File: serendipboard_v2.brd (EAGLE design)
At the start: 34.3 x 48.3 mm, 85 parts, among them IC1 TP4056, IC2 DW01A, IC3 DS3231/SO, J4 USB3076-XX-X_REVC, Q1 FS8205A, Q2 MMBT2222ALT1G, Q3 RUC002N05HZGT116, Q4 DMG3415U, Q5 MMBT2222ALT1G, Q7 RUC002N05HZGT116, Q8 MBT3904DW1T1G, U1 MAX17043, U2 MIC5219 3.3V, U4 9DoF IMU, U5 ESP32-WROOM-32D, U6 FT231XQ-R, U7 MIC5219 3.3V

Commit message: .
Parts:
- renumbered JP1 to VCC, JP2 to AD0, LS1 to BUZZER, S1 to BOOT, S2 to RST, S3 to BTN1, S4 to BTN2, S5 to PWR
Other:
- board text added: "B+"
- board text added: "B-"

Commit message: .
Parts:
- added D2: LTST-C19HE1WT, LTST-C19HE1WT:LED_LTST-C19HE1WT
- added R25, R29, R30: 220, rcl:R0402
- BTN1, BTN2, PWR: value KMR731NGLFS -> (none); device KMR731NGLFS:SW_KMR731NGLFS -> SparkFun-Connectors:1X02
- moved B1 17.9 mm to (12.2, 41.3), turned to 0 degrees
- moved PWR 9.69 mm to (29.6, 29.3), turned to 0 degrees
- moved BTN2 7.42 mm to (29.6, 35.2), turned to 0 degrees
- moved R28 7.03 mm to (20.3, 37.0), turned to 180 degrees
- moved RST 6.10 mm to (30.4, 25.0)
- moved R27 5.72 mm to (20.3, 35.9), turned to 180 degrees
- moved BOOT 5.59 mm to (30.4, 19.8), turned to 270 degrees
- moved BTN1 4.66 mm to (29.6, 32.3), turned to 0 degrees
- moved R26 4.62 mm to (20.3, 34.9), turned to 0 degrees
- moved R9 3.64 mm to (20.3, 38.0), turned to 180 degrees
- moved R19 3.24 mm to (20.3, 33.0), turned to 0 degrees
- moved R20 2.88 mm to (20.3, 34.0), turned to 0 degrees
- moved R13 1.09 mm to (4.70, 35.9), turned to 90 degrees
- moved Q5 0.63 mm to (2.54, 35.6)
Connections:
- new net N$24: D2.1, R25.2
- new net N$26: D2.2, R29.2
- new net N$27: D2.3, R30.2
- net GND: now also BTN1.2, BTN2.2, D2.4, PWR.2; no longer BTN1.3, BTN1.4, BTN2.3, BTN2.4, PWR.3, PWR.4
- net GPIO15: no longer BTN2.2
- net GPIO27: no longer BTN1.2
- net PWR: no longer PWR.2
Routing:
- net GND: track 290.9 -> 238.2 mm, vias 18 -> 16
- net PWR: track 50.3 -> 0.00 mm, vias 4 -> 0
- net EN: track 76.8 -> 34.2 mm, vias 6 -> 5
- net SDA: track 106.7 -> 64.8 mm, vias 6 -> 5
- net GPIO27: track 38.2 -> 2.68 mm, vias 6 -> 1
- net GPIO15: track 48.1 -> 14.3 mm, vias 5 -> 2
- net SCL: track 115.5 -> 89.3 mm
- net VCC: track 91.0 -> 74.9 mm
- net RXD: track 30.4 -> 21.0 mm
- net 3.3V_ESP: track 38.8 -> 29.7 mm
- net MOTOR: track 12.7 -> 8.53 mm
- net N$9: track 4.74 -> 1.14 mm
- net QST: track 64.7 -> 61.4 mm
- net N$13: track 2.14 -> 0.00 mm
- net IO0: track 25.7 -> 24.2 mm
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
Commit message: .
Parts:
- moved R19 0.23 mm to (20.3, 32.8)
- moved R20 0.18 mm to (20.3, 33.9)
- moved R9 0.08 mm to (20.3, 38.0)
- moved R25 0.05 mm to (30.6, 38.4)
- moved R28 0.05 mm to (20.3, 37.0)
- turned R27 to 0 degrees
- turned R30 to 0 degrees
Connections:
- new net BLUE: R30.1, U5.30
- new net GREEN: R29.1, U5.29
- new net N$28: BTN1.1, R28.1
- new net RED: R25.1, U5.28
- net GPIO27: no longer BTN1.1, R28.1
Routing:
- net GPIO27: track 2.68 -> 91.5 mm, vias 1 -> 6
- net GND: track 238.2 -> 305.4 mm, vias 16 -> 18
- net SDA: track 64.8 -> 119.0 mm, vias 5 -> 9
- net EN: track 34.2 -> 66.6 mm, vias 5 -> 9
- net PWR: track 0.00 -> 31.3 mm, vias 0 -> 2
- net N$9: track 1.14 -> 30.4 mm, vias 0 -> 4
- net SCL: track 89.3 -> 117.1 mm, vias 7 -> 11
- net BLUE: track 0.00 -> 24.9 mm, vias 0 -> 2
- net RED: track 0.00 -> 20.3 mm, vias 0 -> 4
- net VCC: track 74.9 -> 90.8 mm
- net 3.3V_ESP: track 29.7 -> 45.5 mm, vias 1 -> 3
- net GREEN: track 0.00 -> 14.7 mm
- net GPIO15: track 14.3 -> 26.6 mm, vias 2 -> 1
- net RXD: track 21.0 -> 29.7 mm, vias 2 -> 3
- net N$24: track 0.00 -> 5.25 mm
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
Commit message: .
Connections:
- removed net N$28: BTN1.1, R28.1
- net GPIO27: now also BTN1.1, R28.1
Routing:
- net GPIO27: track 91.5 -> 94.3 mm
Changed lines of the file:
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@@
 <wire x1="5.2435" y1="24.284" x2="4.7625" y2="24.765" width="0.254" layer="16"/>
 <wire x1="10.09390625" y1="28.2575" x2="6.12040625" y2="24.284" width="0.254" layer="16"/>
+<contactref element="R28" pad="1"/>
+<contactref element="BTN1" pad="1"/>
+<wire x1="19.82" y1="37.0078" x2="19.00295625" y2="37.0078" width="0.254" layer="16"/>
+<wire x1="29.591" y1="32.258" x2="30.988" y2="33.655" width="0.254" layer="1"/>
 </signal>
 <signal name="GPIO15">
@@
 <wire x1="30.107" y1="38.4209875" x2="30.107" y2="38.4302" width="0.254" layer="1"/>
 </signal>
-<signal name="N$28">
-<contactref element="R28" pad="1"/>
-<contactref element="BTN1" pad="1"/>
-<wire x1="19.82" y1="37.0078" x2="29.591" y2="32.258" width="0" layer="19" extent="16-16"/>
-</signal>
 </signals>

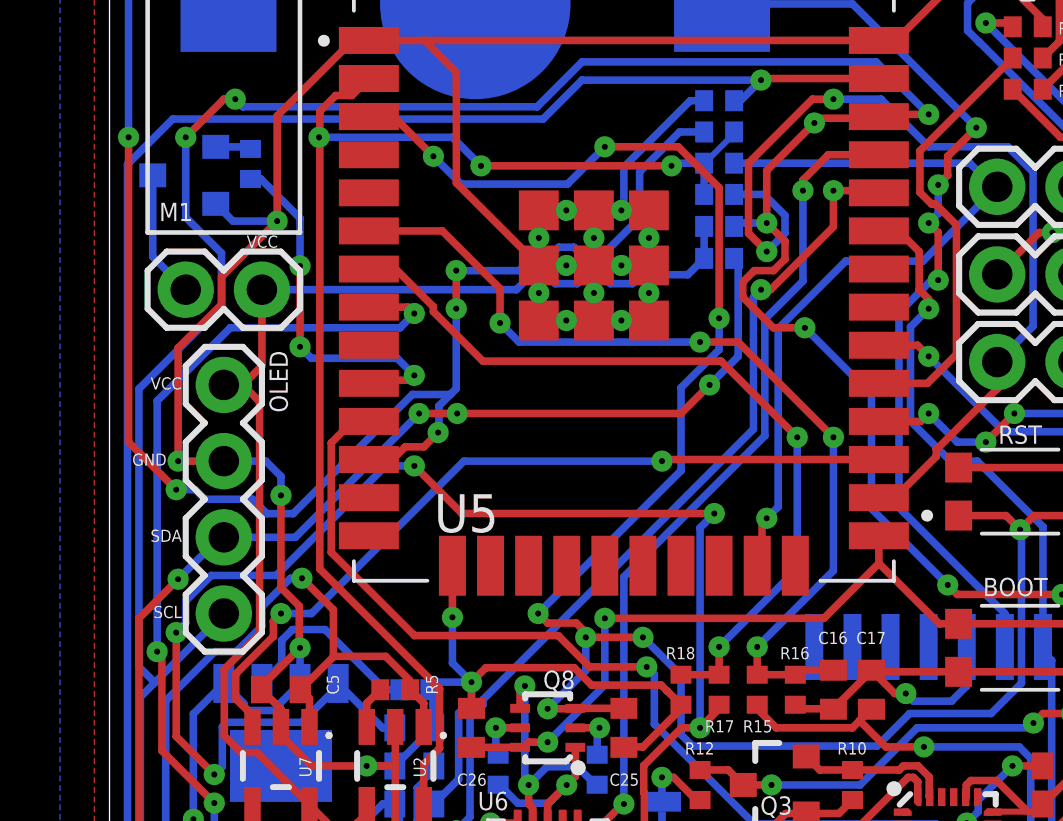
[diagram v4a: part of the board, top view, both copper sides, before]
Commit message: Update serendipboard_v2.brd
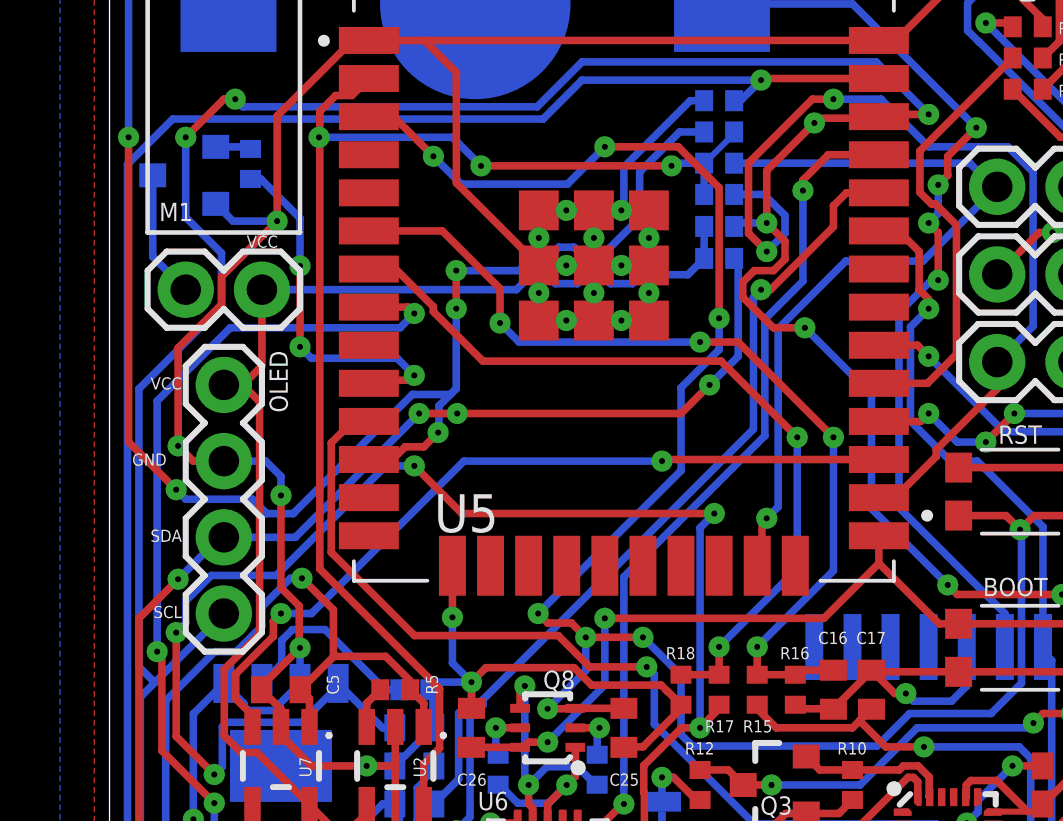
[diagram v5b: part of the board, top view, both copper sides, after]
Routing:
- net RXD: track 29.7 -> 29.3 mm, vias 3 -> 2
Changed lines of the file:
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@@
 <wire x1="5.588" y1="34.036" x2="3.7338" y2="32.1818" width="0.254" layer="1"/>
 <wire x1="3.7338" y1="32.1818" x2="3.7338" y2="31.25550625" width="0.254" layer="1"/>
-<wire x1="2.286" y1="29.80770625" x2="2.286" y2="26.035" width="0.254" layer="1"/>
+<wire x1="2.286" y1="29.80770625" x2="2.286" y2="26.543" width="0.254" layer="1"/>
 <wire x1="3.7338" y1="31.25550625" x2="2.286" y2="29.80770625" width="0.254" layer="1"/>
-<via x="2.286" y="26.035" extent="1-16" drill="0.2"/>
-<wire x1="2.286" y1="26.035" x2="3.81" y2="26.035" width="0.254" layer="1"/>
+<via x="2.286" y="26.543" extent="1-16" drill="0.2"/>
+<wire x1="2.794" y1="26.035" x2="3.81" y2="26.035" width="0.254" layer="1"/>
+<wire x1="2.794" y1="26.035" x2="2.286" y2="26.543" width="0.254" layer="1"/>
 <wire x1="17.0625" y1="30.723" x2="17.98" y2="30.723" width="0.254" layer="1"/>
 <wire x1="10.66" y1="18.415" x2="10.914" y2="18.669" width="0.254" layer="16"/>
@@
 <wire x1="14.2875" y1="20.955" x2="19.05" y2="25.7175" width="0.254" layer="16"/>
 <wire x1="14.605" y1="20.6375" x2="14.2875" y2="20.955" width="0.254" layer="1"/>
-<wire x1="15.5575" y1="20.6375" x2="14.605" y2="20.6375" width="0.254" layer="1"/>
-<wire x1="15.875" y1="20.32" x2="15.5575" y2="20.6375" width="0.254" layer="1"/>
-<wire x1="15.875" y1="20.32" x2="15.875" y2="20.16125" width="0.254" layer="1"/>
 <via x="10.795" y="36.195" extent="1-16" drill="0.2"/>
 <via x="16.51" y="36.5125" extent="1-16" drill="0.2"/>
@@
 <wire x1="15.267" y1="35.2695" x2="11.7205" y2="35.2695" width="0.254" layer="16"/>
 <wire x1="11.7205" y1="35.2695" x2="10.795" y2="36.195" width="0.254" layer="16"/>
+<wire x1="15.875" y1="20.16125" x2="15.39875" y2="20.6375" width="0.254" layer="1"/>
+<wire x1="15.39875" y1="20.6375" x2="14.605" y2="20.6375" width="0.254" layer="1"/>
 </signal>
 <signal name="IO0">
@@
 <via x="11.557" y="13.716" extent="1-16" drill="0.2"/>
 <wire x1="11.557" y1="13.716" x2="12.017" y2="14.176" width="0.254" layer="16"/>
-<via x="24.13" y="35.052" extent="1-16" drill="0.2"/>
 <wire x1="12.017" y1="14.176" x2="12.017" y2="17.478" width="0.254" layer="16"/>
-<wire x1="24.13" y1="35.052" x2="25.571" y2="35.052" width="0.254" layer="1"/>
-<wire x1="25.571" y1="35.052" x2="25.645" y2="34.978" width="0.254" layer="1"/>
 <wire x1="12.017" y1="17.478" x2="12.446" y2="17.907" width="0.254" layer="16"/>
 <wire x1="12.446" y1="17.907" x2="12.446" y2="18.0840875" width="0.254" layer="16"/>
@@
 <via x="21.717" y="31.75" extent="1-16" drill="0.2"/>
 <wire x1="21.717" y1="31.75" x2="22.0361625" y2="31.75" width="0.254" layer="1"/>
-<wire x1="22.0361625" y1="31.75" x2="24.13" y2="33.8438375" width="0.254" layer="1"/>
-<wire x1="24.13" y1="33.8438375" x2="24.13" y2="35.052" width="0.254" layer="1"/>
+<wire x1="24.13" y1="33.8438375" x2="22.0361625" y2="31.75" width="0.254" layer="1"/>
+<wire x1="24.13" y1="34.544" x2="24.13" y2="33.8438375" width="0.254" layer="1"/>
+<wire x1="24.13" y1="34.544" x2="24.564" y2="34.978" width="0.254" layer="1"/>
+<wire x1="24.564" y1="34.978" x2="25.645" y2="34.978" width="0.254" layer="1"/>
 </signal>
 <signal name="N$15">
@@
 <wire x1="10.98075" y1="27.0145" x2="10.95375" y2="26.9875" width="0.254" layer="16"/>
 <wire x1="11.557" y1="28.45059375" x2="11.396953125" y2="28.290546875" width="0.254" layer="16"/>
-<wire x1="11.396953125" y1="28.290546875" x2="10.98075" y2="27.87434375" width="0.254" layer="16"/>
+<wire x1="11.36390625" y1="28.2575" x2="10.98075" y2="27.87434375" width="0.254" layer="16"/>
 <wire x1="10.98075" y1="27.87434375" x2="10.98075" y2="27.0145" width="0.254" layer="16"/>
-<wire x1="2.8575" y1="25.0825" x2="2.2225" y2="25.0825" width="0.254" layer="16"/>
-<wire x1="3.175" y1="24.765" x2="2.8575" y2="25.0825" width="0.254" layer="16"/>
+<wire x1="2.54" y1="24.765" x2="2.2225" y2="25.0825" width="0.254" layer="16"/>
 <via x="31.4325" y="33.655" extent="1-16" drill="0.2"/>
 <via x="0.635" y="36.83" extent="1-16" drill="0.2"/>
@@
 <wire x1="0.635" y1="26.67" x2="0.635" y2="36.83" width="0.254" layer="1"/>
 <wire x1="11.396953125" y1="28.290546875" x2="11.36390625" y2="28.2575" width="0.254" layer="16"/>
-<wire x1="4.7625" y1="24.765" x2="3.175" y2="24.765" width="0.254" layer="16"/>
+<wire x1="4.7625" y1="24.765" x2="2.54" y2="24.765" width="0.254" layer="16"/>
 <wire x1="11.36390625" y1="28.2575" x2="10.09390625" y2="28.2575" width="0.254" layer="16"/>
 <wire x1="6.12040625" y1="24.284" x2="5.2435" y2="24.284" width="0.254" layer="16"/>
